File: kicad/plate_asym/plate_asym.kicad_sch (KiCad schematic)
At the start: 69 parts, among them SW1 EC_SW

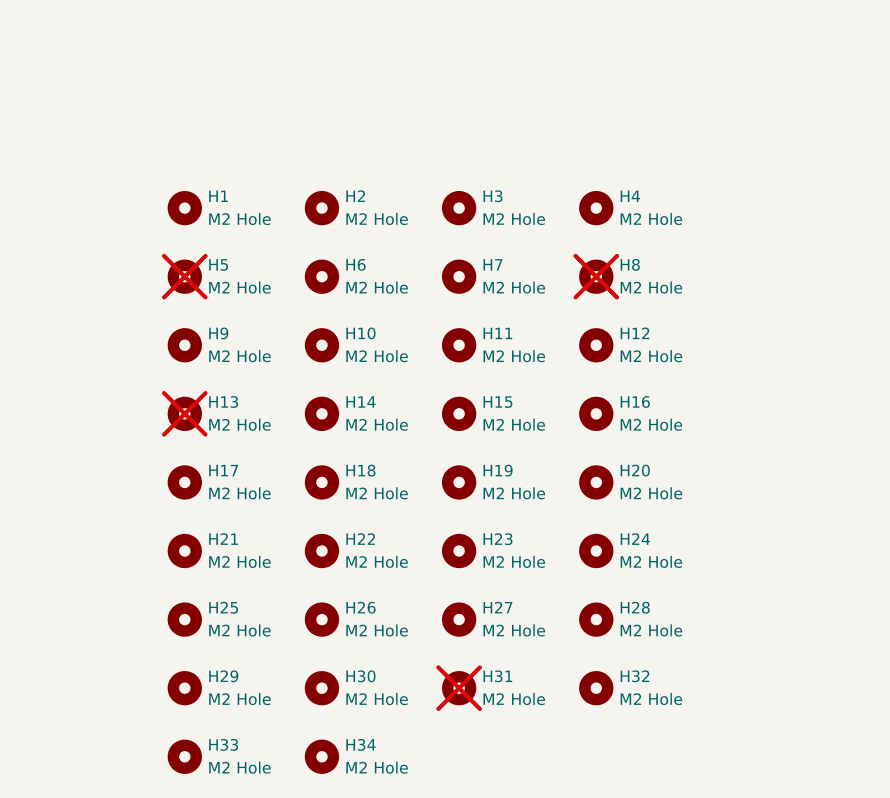
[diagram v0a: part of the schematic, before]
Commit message: Making production plates
- Change EC mounting hole size from 2.2mm clearance to 1.6mm for M2
  tapping
- Reduce hole count for cost reduction
- Add drilling/fabrication notes
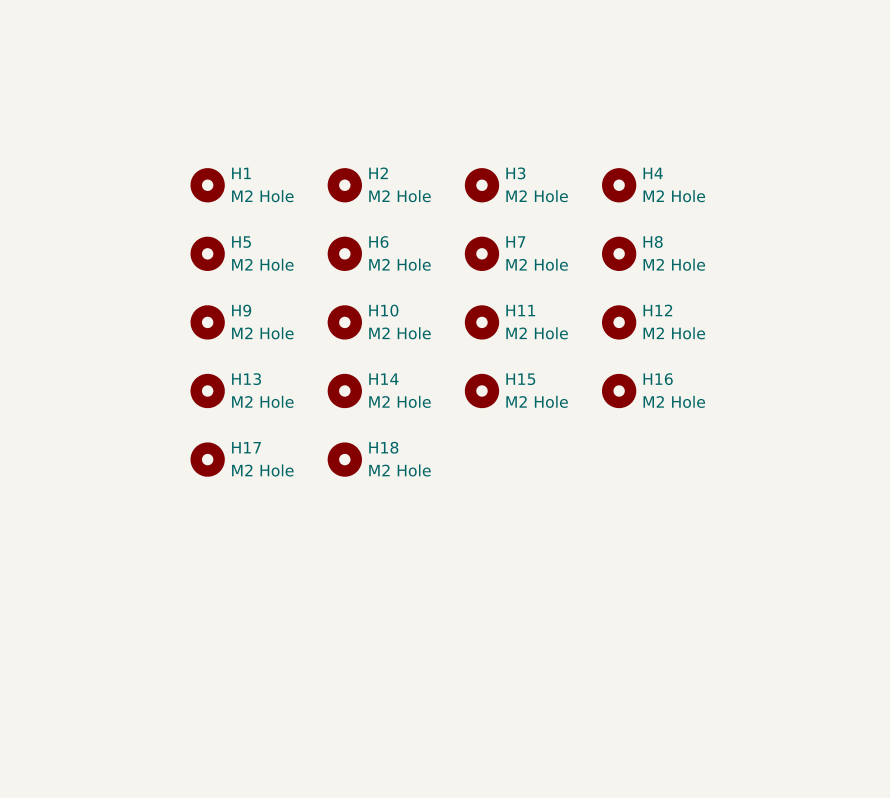
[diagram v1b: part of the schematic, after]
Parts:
- removed H11, H13, H15, H16, H17, H18, H19, H20, H24, H25, H28, H31, H33, H5, H6, H8: M2 Hole, capacitive_sensors:MountingHole_2.2mm_M2, symbol Mechanical:MountingHole
- H1, H2, H3, H4: footprint capacitive_sensors:MountingHole_2.2mm_M2 -> capacitive_sensors:MountingHole_1.6mm_M2_tapped
- H10: renamed from H21; footprint capacitive_sensors:MountingHole_2.2mm_M2 -> capacitive_sensors:MountingHole_1.6mm_M2_tapped
- H11: renamed from H22; footprint capacitive_sensors:MountingHole_2.2mm_M2 -> capacitive_sensors:MountingHole_1.6mm_M2_tapped
- H12: renamed from H23; footprint capacitive_sensors:MountingHole_2.2mm_M2 -> capacitive_sensors:MountingHole_1.6mm_M2_tapped
- H13: renamed from H26; footprint capacitive_sensors:MountingHole_2.2mm_M2 -> capacitive_sensors:MountingHole_1.6mm_M2_tapped
- H14: renamed from H27; footprint capacitive_sensors:MountingHole_2.2mm_M2 -> capacitive_sensors:MountingHole_1.6mm_M2_tapped
- H15: renamed from H29; footprint capacitive_sensors:MountingHole_2.2mm_M2 -> capacitive_sensors:MountingHole_1.6mm_M2_tapped
- H16: renamed from H30; footprint capacitive_sensors:MountingHole_2.2mm_M2 -> capacitive_sensors:MountingHole_1.6mm_M2_tapped
- H17: renamed from H32; footprint capacitive_sensors:MountingHole_2.2mm_M2 -> capacitive_sensors:MountingHole_1.6mm_M2_tapped
- H18: renamed from H34; footprint capacitive_sensors:MountingHole_2.2mm_M2 -> capacitive_sensors:MountingHole_1.6mm_M2_tapped
- H5: renamed from H7; footprint capacitive_sensors:MountingHole_2.2mm_M2 -> capacitive_sensors:MountingHole_1.6mm_M2_tapped
- H6: renamed from H9; footprint capacitive_sensors:MountingHole_2.2mm_M2 -> capacitive_sensors:MountingHole_1.6mm_M2_tapped
- H7: renamed from H10; footprint capacitive_sensors:MountingHole_2.2mm_M2 -> capacitive_sensors:MountingHole_1.6mm_M2_tapped
- H8: renamed from H12; footprint capacitive_sensors:MountingHole_2.2mm_M2 -> capacitive_sensors:MountingHole_1.6mm_M2_tapped
- H9: renamed from H14; footprint capacitive_sensors:MountingHole_2.2mm_M2 -> capacitive_sensors:MountingHole_1.6mm_M2_tapped
- SW1: footprint capacitive_sensors:plate_cut_1U_topre -> capacitive_sensors:plate_cut_2U_topre
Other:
- moved on the sheet: H1, H10, H11, H12, H13, H14, H15, H16, H17, H18, H2, H3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

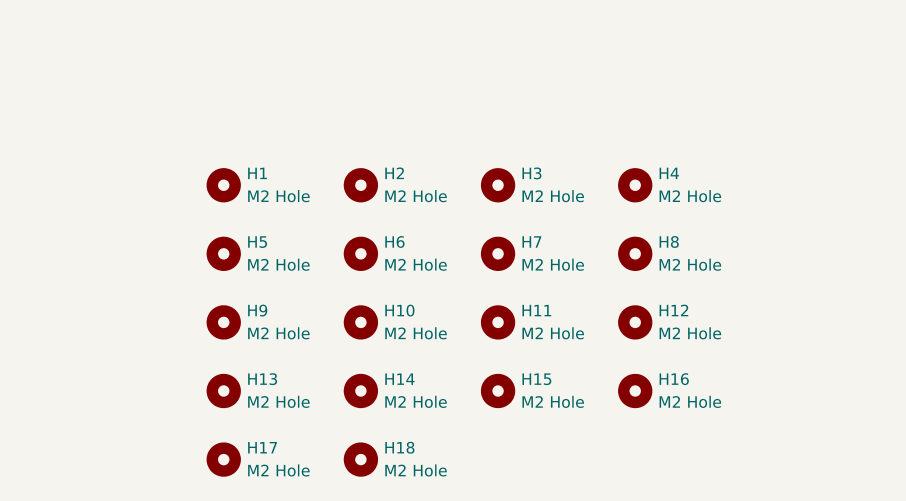
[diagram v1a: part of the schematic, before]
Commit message: Clean up after prototyping
- Doc update
- remove uncessary files
- remove two more mounting holes in the "chiffre gap" area
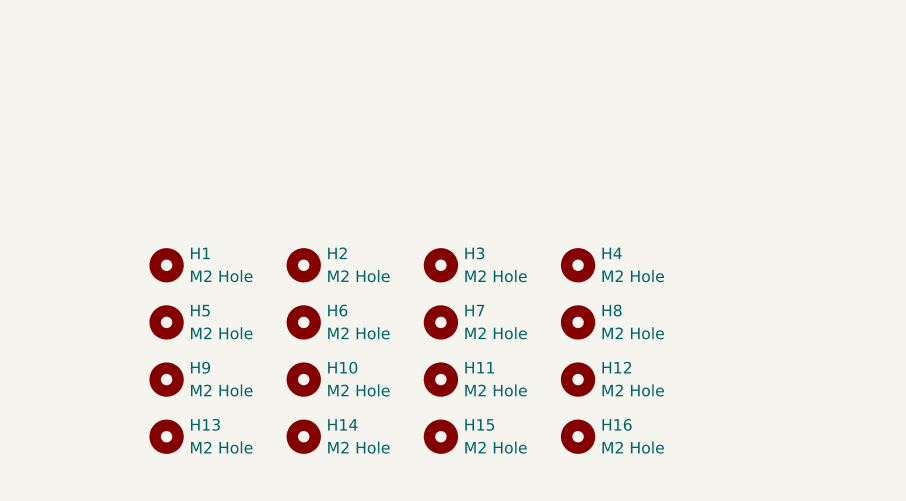
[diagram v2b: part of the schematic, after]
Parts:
- removed H17, H18: M2 Hole, capacitive_sensors:MountingHole_1.6mm_M2_tapped, symbol Mechanical:MountingHole

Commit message: Remove extra mounting holes from PCB and update version number.
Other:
- title: Le Capybara -> Le Capybara Plate (Asymmetric)
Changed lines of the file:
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@@
   (paper "A4")
   (title_block
-    (title "Le Capybara")
-    (date "2023-07-08")
-    (rev "0.2")
+    (title "Le Capybara Plate (Asymmetric)")
+    (date "2024-02-21")
+    (rev "1.0")
     (company "sporkus")
   )
